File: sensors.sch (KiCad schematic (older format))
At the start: 11 parts, among them U11 TSOP753, U12 LIS2HH12, U8 VL53L0X

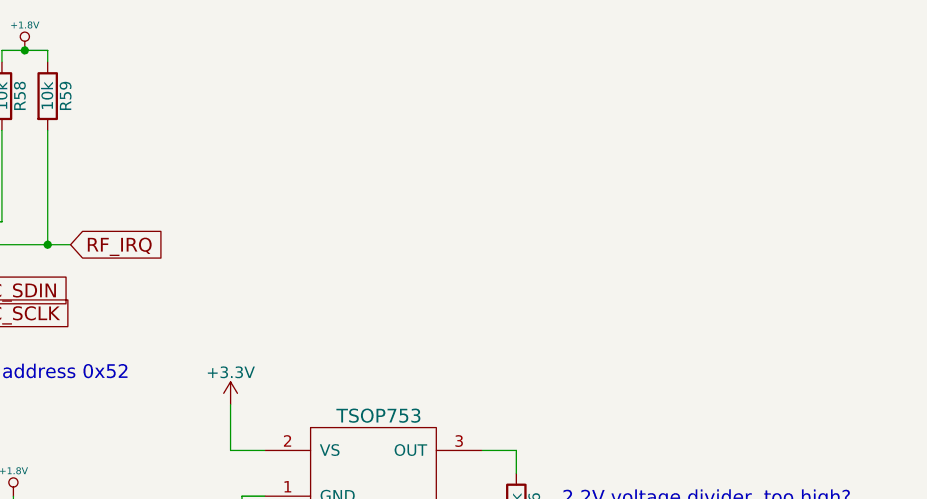
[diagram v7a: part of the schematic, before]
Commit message: about to remove 2.4ghz radio, which complicates compliance and is redundant to MIDI over BLE over USB
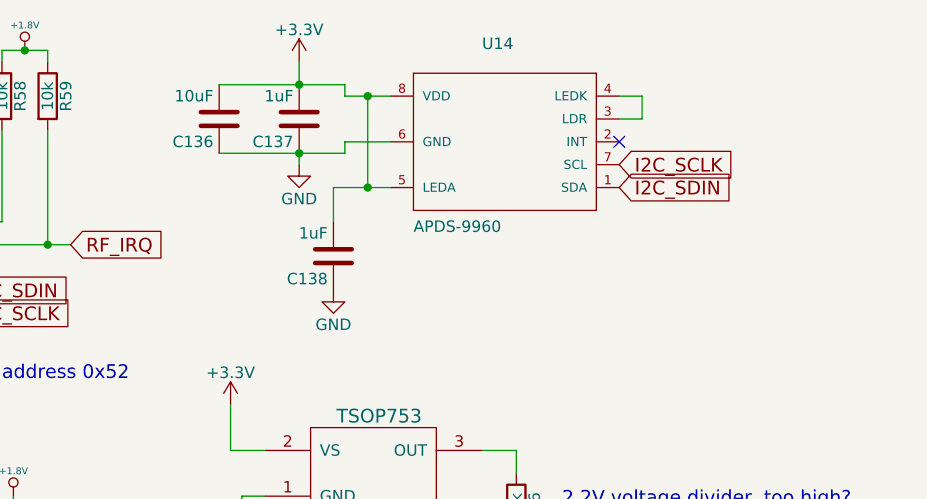
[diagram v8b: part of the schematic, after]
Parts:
- added C136: 10uF, Capacitors_SMD:C_0805, symbol C
- added C137, C138: 1uF, Capacitors_SMD:C_0603, symbol C
- added U14: APDS-9960, DFTcustom:APDS_9960, symbol APDS-9960
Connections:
- net +3V3: now also C136.2, C137.2, C138.2, U14.5 (LEDA), U14.8 (VDD)
- net GND: now also C136.1, C137.1, C138.1, U14.6 (GND)
- net I2C_SCLK: now also U14.7 (SCL)
- net I2C_SDIN: now also U14.1 (SDA)
- new net: U14.3 (LDR), U14.4 (LEDK)
- no-connect marks 3 -> 4
